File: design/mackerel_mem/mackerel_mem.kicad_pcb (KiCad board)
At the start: 2 copper layers, 99.1 x 99.1 mm, 9 parts, among them U1 AS6C4008-55PCN, U2 AS6C4008-55PCN, U3 AS6C4008-55PCN, U4 AS6C4008-55PCN, U5 AS6C4008-55PCN, U6 AS6C4008-55PCN, U7 AS6C4008-55PCN, U8 AS6C4008-55PCN, U9 GAL16V8

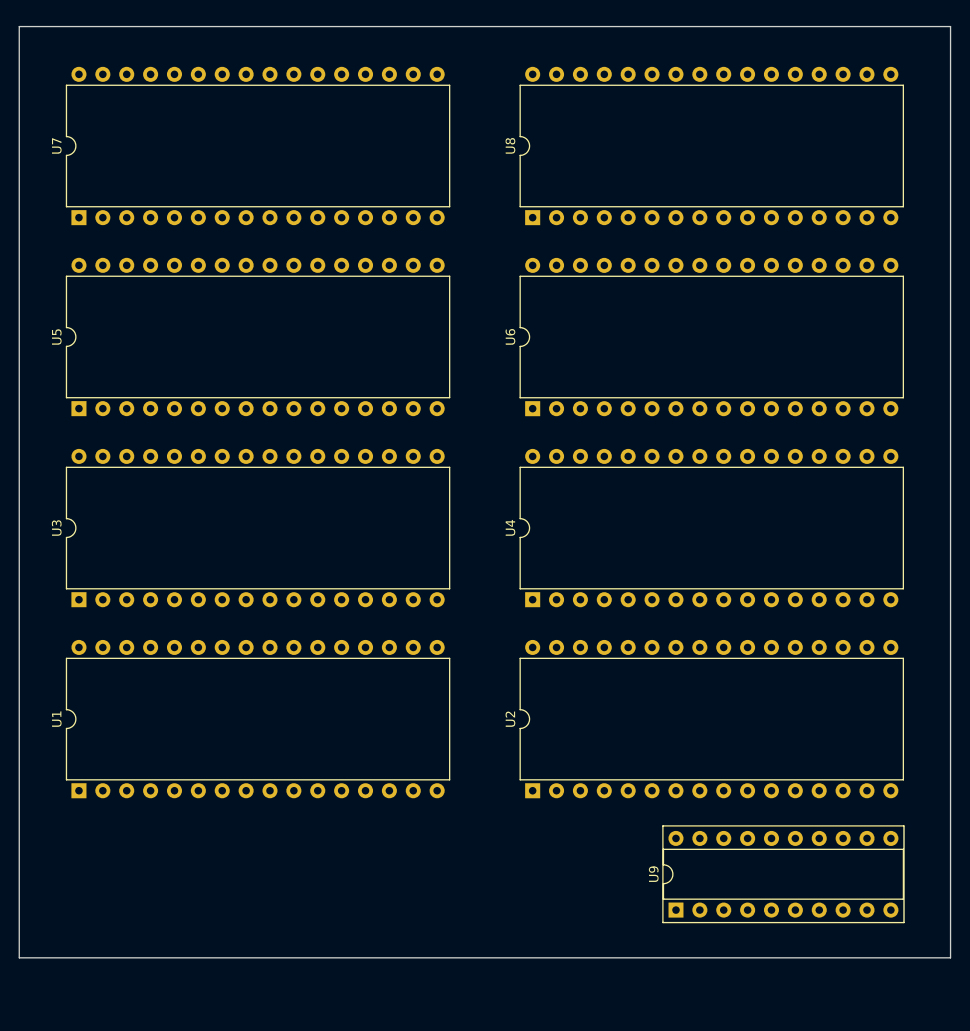
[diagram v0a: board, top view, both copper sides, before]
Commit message: Defined system bus pinout and GAL decoding schematic
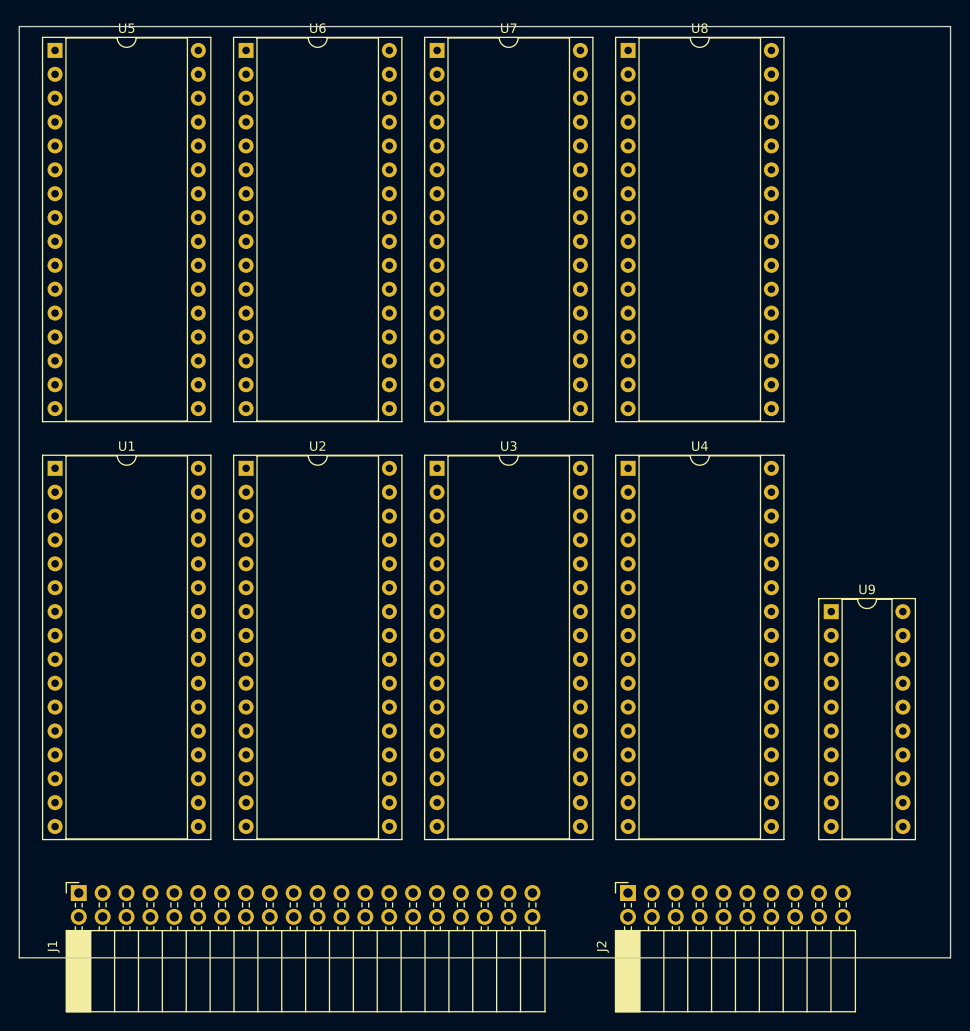
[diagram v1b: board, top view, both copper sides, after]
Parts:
- added J1: Conn_02x20_Odd_Even, Connector_PinSocket_2.54mm:PinSocket_2x20_P2.54mm_Horizontal, F.Cu at (54.6, 130.3)
- added J2: Conn_02x10_Odd_Even, Connector_PinSocket_2.54mm:PinSocket_2x10_P2.54mm_Horizontal, F.Cu at (113.0, 130.3)
- U1, U2, U3, U4, U5, U6, U7: footprint Package_DIP:DIP-32_W15.24mm -> Package_DIP:DIP-32_W15.24mm_Socket
- U8: value AS6C4008-55PCN -> SST39SF040; footprint Package_DIP:DIP-32_W15.24mm -> Package_DIP:DIP-32_W15.24mm_Socket
- moved U6 48.8 mm to (72.4, 40.6), turned to 0 degrees
- moved U2 45.9 mm to (72.4, 85.1), turned to 0 degrees
- moved U7 42.0 mm to (92.7, 40.6), turned to 0 degrees
- moved U3 40.6 mm to (92.7, 85.1), turned to 0 degrees
- moved U5 38.2 mm to (52.1, 40.6), turned to 0 degrees
- moved U9 35.8 mm to (134.6, 100.3), turned to 0 degrees
- moved U1 34.4 mm to (52.1, 85.1), turned to 0 degrees
- moved U8 20.5 mm to (113.0, 40.6), turned to 0 degrees
- moved U4 17.3 mm to (113.0, 85.1), turned to 0 degrees
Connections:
- U8 pad 1: /A18 -> unconnected-(U8-Pad1)
- U8 pad 10: /A2 -> unconnected-(U8-Pad10)
- U8 pad 11: /A1 -> unconnected-(U8-Pad11)
- U8 pad 12: /A0 -> unconnected-(U8-Pad12)
- U8 pad 13: /D0 -> unconnected-(U8-Pad13)
- U8 pad 14: /D1 -> unconnected-(U8-Pad14)
- U8 pad 15: /D2 -> unconnected-(U8-Pad15)
- U8 pad 17: /D3 -> unconnected-(U8-Pad17)
- U8 pad 18: /D4 -> unconnected-(U8-Pad18)
- U8 pad 19: /D5 -> unconnected-(U8-Pad19)
- U8 pad 2: /A16 -> unconnected-(U8-Pad2)
- U8 pad 20: /D6 -> unconnected-(U8-Pad20)
- U8 pad 21: /D7 -> unconnected-(U8-Pad21)
- U8 pad 22: /CE7 -> unconnected-(U8-Pad22)
- U8 pad 23: /A10 -> unconnected-(U8-Pad23)
- U8 pad 24: GND -> unconnected-(U8-Pad24)
- U8 pad 25: /A11 -> unconnected-(U8-Pad25)
- U8 pad 26: /A9 -> unconnected-(U8-Pad26)
- U8 pad 27: /A8 -> unconnected-(U8-Pad27)
- U8 pad 28: /A13 -> unconnected-(U8-Pad28)
- U8 pad 29: /RW -> unconnected-(U8-Pad29)
- U8 pad 3: /A14 -> unconnected-(U8-Pad3)
- U8 pad 30: /A17 -> unconnected-(U8-Pad30)
- U8 pad 31: /A15 -> unconnected-(U8-Pad31)
- U8 pad 32: +5V -> VCC
- U8 pad 4: /A12 -> unconnected-(U8-Pad4)
- U8 pad 5: /A7 -> unconnected-(U8-Pad5)
- U8 pad 6: /A6 -> unconnected-(U8-Pad6)
- U8 pad 7: /A5 -> unconnected-(U8-Pad7)
- U8 pad 8: /A4 -> unconnected-(U8-Pad8)
- U8 pad 9: /A3 -> unconnected-(U8-Pad9)
- U9 pad 1: unconnected-(U9-Pad1) -> /~{CS_ROM}
